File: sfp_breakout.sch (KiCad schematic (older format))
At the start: 12 parts

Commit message: Started some board layout
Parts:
- gave numbers to parts that had none: 12
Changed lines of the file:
@@
 LIBS:valves
 LIBS:visgence_parts
+LIBS:sfp_breakout-cache
 EELAYER 25 0
 EELAYER END
@@
 $EndDescr
 $Comp
-L SFP U?
+L SFP U1
 U 1 1 5A14503B
 P 2925 2550
-F 0 "U?" H 2925 3150 60  0000 C CNN
+F 0 "U1" H 2925 3150 60  0000 C CNN
 F 1 "SFP" H 2925 2000 60  0000 C CNN
 F 2 "" H 2925 2550 60  0001 C CNN
@@
 	4075 2350 4750 2350
 $Comp
-L C C?
+L C C2
 U 1 1 5A1450E2
 P 4425 2500
-F 0 "C?" H 4450 2600 50  0000 L CNN
+F 0 "C2" H 4450 2600 50  0000 L CNN
 F 1 "0.1u" H 4450 2400 50  0000 L CNN
 F 2 "" H 4463 2350 50  0001 C CNN
@@
 $EndComp
 $Comp
-L L L?
+L L L1
 U 1 1 5A14512D
 P 4900 2350
-F 0 "L?" V 4850 2350 50  0000 C CNN
+F 0 "L1" V 4850 2350 50  0000 C CNN
 F 1 "1u" V 4975 2350 50  0000 C CNN
 F 2 "" H 4900 2350 50  0001 C CNN
@@
 Connection ~ 4425 2350
 $Comp
-L C C?
+L C C1
 U 1 1 5A1451E0
 P 4275 3075
-F 0 "C?" H 4300 3175 50  0000 L CNN
+F 0 "C1" H 4300 3175 50  0000 L CNN
 F 1 "0.1u" H 4300 2975 50  0000 L CNN
 F 2 "" H 4313 2925 50  0001 C CNN
@@
 $EndComp
 $Comp
-L C C?
+L C C3
 U 1 1 5A145214
 P 4625 3075
-F 0 "C?" H 4650 3175 50  0000 L CNN
+F 0 "C3" H 4650 3175 50  0000 L CNN
 F 1 "10u" H 4650 2975 50  0000 L CNN
 F 2 "" H 4663 2925 50  0001 C CNN
@@
 Connection ~ 4275 2925
 $Comp
-L L L?
+L L L2
 U 1 1 5A14529D
 P 4900 2925
-F 0 "L?" V 4850 2925 50  0000 C CNN
+F 0 "L2" V 4850 2925 50  0000 C CNN
 F 1 "1u" V 4975 2925 50  0000 C CNN
 F 2 "" H 4900 2925 50  0001 C CNN
@@
 	5050 2350 5050 2925
 $Comp
-L C C?
+L C C4
 U 1 1 5A145370
 P 5275 3075
-F 0 "C?" H 5300 3175 50  0000 L CNN
+F 0 "C4" H 5300 3175 50  0000 L CNN
 F 1 "0.1u" H 5300 2975 50  0000 L CNN
 F 2 "" H 5313 2925 50  0001 C CNN
@@
 $EndComp
 $Comp
-L C C?
+L C C5
 U 1 1 5A1453AF
 P 5625 3075
-F 0 "C?" H 5650 3175 50  0000 L CNN
+F 0 "C5" H 5650 3175 50  0000 L CNN
 F 1 "10u" H 5650 2975 50  0000 L CNN
 F 2 "" H 5663 2925 50  0001 C CNN
@@
 Connection ~ 5275 2925
 $Comp
-L GND #PWR?
+L GND #PWR6
 U 1 1 5A14541F
 P 4275 3300
-F 0 "#PWR?" H 4275 3050 50  0001 C CNN
+F 0 "#PWR6" H 4275 3050 50  0001 C CNN
 F 1 "GND" H 4275 3150 50  0000 C CNN
 F 2 "" H 4275 3300 50  0001 C CNN
@@
 $EndComp
 $Comp
-L GND #PWR?
+L GND #PWR7
 U 1 1 5A145449
 P 4425 2700
-F 0 "#PWR?" H 4425 2450 50  0001 C CNN
+F 0 "#PWR7" H 4425 2450 50  0001 C CNN
 F 1 "GND" H 4425 2550 50  0000 C CNN
 F 2 "" H 4425 2700 50  0001 C CNN
@@
 	4425 2650 4425 2700
 $Comp
-L GND #PWR?
+L GND #PWR8
 U 1 1 5A145590
 P 4625 3300
-F 0 "#PWR?" H 4625 3050 50  0001 C CNN
+F 0 "#PWR8" H 4625 3050 50  0001 C CNN
 F 1 "GND" H 4625 3150 50  0000 C CNN
 F 2 "" H 4625 3300 50  0001 C CNN
@@
 $EndComp
 $Comp
-L GND #PWR?
+L GND #PWR9
 U 1 1 5A1455B3
 P 5275 3300
-F 0 "#PWR?" H 5275 3050 50  0001 C CNN
+F 0 "#PWR9" H 5275 3050 50  0001 C CNN
 F 1 "GND" H 5275 3150 50  0000 C CNN
 F 2 "" H 5275 3300 50  0001 C CNN
@@
 $EndComp
 $Comp
-L GND #PWR?
+L GND #PWR11
 U 1 1 5A1455D6
 P 5625 3300
-F 0 "#PWR?" H 5625 3050 50  0001 C CNN
+F 0 "#PWR11" H 5625 3050 50  0001 C CNN
 F 1 "GND" H 5625 3150 50  0000 C CNN
 F 2 "" H 5625 3300 50  0001 C CNN
@@
 	5625 3225 5625 3300
 $Comp
-L +3.3V #PWR?
+L +3.3V #PWR10
 U 1 1 5A145656
 P 5625 2675
-F 0 "#PWR?" H 5625 2525 50  0001 C CNN
+F 0 "#PWR10" H 5625 2525 50  0001 C CNN
 F 1 "+3.3V" H 5625 2815 50  0000 C CNN
 F 2 "" H 5625 2675 50  0001 C CNN
@@
 	5625 2925 5625 2675
 $Comp
-L GND #PWR?
+L GND #PWR3
 U 1 1 5A145883
 P 3700 3075
-F 0 "#PWR?" H 3700 2825 50  0001 C CNN
+F 0 "#PWR3" H 3700 2825 50  0001 C CNN
 F 1 "GND" H 3700 2925 50  0000 C CNN
 F 2 "" H 3700 3075 50  0001 C CNN
@@
 	3700 3000 3700 3075
 $Comp
-L GND #PWR?
+L GND #PWR2
 U 1 1 5A1458D2
 P 2050 3050
-F 0 "#PWR?" H 2050 2800 50  0001 C CNN
+F 0 "#PWR2" H 2050 2800 50  0001 C CNN
 F 1 "GND" H 2050 2900 50  0000 C CNN
 F 2 "" H 2050 3050 50  0001 C CNN
@@
 Connection ~ 2050 3000
 $Comp
-L GND #PWR?
+L GND #PWR1
 U 1 1 5A14597C
 P 1800 2200
-F 0 "#PWR?" H 1800 1950 50  0001 C CNN
+F 0 "#PWR1" H 1800 1950 50  0001 C CNN
 F 1 "GND" H 1800 2050 50  0000 C CNN
 F 2 "" H 1800 2200 50  0001 C CNN
@@
 	1800 2100 2175 2100
 $Comp
-L GND #PWR?
+L GND #PWR5
 U 1 1 5A1459D9
 P 4025 2150
-F 0 "#PWR?" H 4025 1900 50  0001 C CNN
+F 0 "#PWR5" H 4025 1900 50  0001 C CNN
 F 1 "GND" H 4025 2000 50  0000 C CNN
 F 2 "" H 4025 2150 50  0001 C CNN
@@
 	3675 2900 3625 2900
 $Comp
-L GND #PWR?
+L GND #PWR4
 U 1 1 5A145C02
 P 3950 3075
-F 0 "#PWR?" H 3950 2825 50  0001 C CNN
+F 0 "#PWR4" H 3950 2825 50  0001 C CNN
 F 1 "GND" H 3950 2925 50  0000 C CNN
 F 2 "" H 3950 3075 50  0001 C CNN
@@
 	3950 2700 3950 3075
 $Comp
-L Conn_Coaxial J?
+L Conn_Coaxial J1
 U 1 1 5A145ECA
 P 7650 1950
-F 0 "J?" H 7660 2070 50  0000 C CNN
+F 0 "J1" H 7660 2070 50  0000 C CNN
 F 1 "TD-" V 7765 1950 50  0000 C CNN
 F 2 "" H 7650 1950 50  0001 C CNN
@@
 $EndComp
 $Comp
-L Conn_Coaxial J?
+L Conn_Coaxial J2
 U 1 1 5A1460BD
 P 7650 2400
-F 0 "J?" H 7660 2520 50  0000 C CNN
+F 0 "J2" H 7660 2520 50  0000 C CNN
 F 1 "TD+" V 7765 2400 50  0000 C CNN
 F 2 "" H 7650 2400 50  0001 C CNN
@@
 $EndComp
 $Comp
-L Conn_Coaxial J?
+L Conn_Coaxial J3
 U 1 1 5A14613D
 P 7650 3050
-F 0 "J?" H 7660 3170 50  0000 C CNN
+F 0 "J3" H 7660 3170 50  0000 C CNN
 F 1 "RD+" V 7765 3050 50  0000 C CNN
 F 2 "" H 7650 3050 50  0001 C CNN
@@
 $EndComp
 $Comp
-L Conn_Coaxial J?
+L Conn_Coaxial J4
 U 1 1 5A1461B6
 P 7650 3525
-F 0 "J?" H 7660 3645 50  0000 C CNN
+F 0 "J4" H 7660 3645 50  0000 C CNN
 F 1 "RD-" V 7765 3525 50  0000 C CNN
 F 2 "" H 7650 3525 50  0001 C CNN
@@
 	7500 3525 7300 3525
 $Comp
-L GND #PWR?
+L GND #PWR12
 U 1 1 5A146933
 P 8025 2250
-F 0 "#PWR?" H 8025 2000 50  0001 C CNN
+F 0 "#PWR12" H 8025 2000 50  0001 C CNN
 F 1 "GND" H 8025 2100 50  0000 C CNN
 F 2 "" H 8025 2250 50  0001 C CNN
@@
 	8025 2150 8025 2250
 $Comp
-L GND #PWR?
+L GND #PWR13
 U 1 1 5A1469CA
 P 8025 2650
-F 0 "#PWR?" H 8025 2400 50  0001 C CNN
+F 0 "#PWR13" H 8025 2400 50  0001 C CNN
 F 1 "GND" H 8025 2500 50  0000 C CNN
 F 2 "" H 8025 2650 50  0001 C CNN
@@
 	8025 2600 8025 2650
 $Comp
-L GND #PWR?
+L GND #PWR14
 U 1 1 5A146A7B
 P 8025 3325
-F 0 "#PWR?" H 8025 3075 50  0001 C CNN
+F 0 "#PWR14" H 8025 3075 50  0001 C CNN
 F 1 "GND" H 8025 3175 50  0000 C CNN
 F 2 "" H 8025 3325 50  0001 C CNN
@@
 	8025 3250 8025 3325
 $Comp
-L GND #PWR?
+L GND #PWR15
 U 1 1 5A146AF2
 P 8025 3775
-F 0 "#PWR?" H 8025 3525 50  0001 C CNN
+F 0 "#PWR15" H 8025 3525 50  0001 C CNN
 F 1 "GND" H 8025 3625 50  0000 C CNN
 F 2 "" H 8025 3775 50  0001 C CNN

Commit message: Changed out SMA connector
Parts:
- C1, C2, C3, C4, C5: footprint (none) -> Capacitors_SMD:C_0603
- J1, J2, J3, J4: footprint (none) -> visgence_parts:CON-SMA-EDGE
- L1, L2: footprint (none) -> visgence_parts:SM0603_VIS
- U1: footprint (none) -> visgence_parts:UE75-A20
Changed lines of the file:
@@
 F 0 "U1" H 2925 3150 60  0000 C CNN
 F 1 "SFP" H 2925 2000 60  0000 C CNN
-F 2 "" H 2925 2550 60  0001 C CNN
+F 2 "visgence_parts:UE75-A20" H 2925 2550 60  0001 C CNN
 F 3 "" H 2925 2550 60  0001 C CNN
 	1    2925 2550
@@
 F 0 "C2" H 4450 2600 50  0000 L CNN
 F 1 "0.1u" H 4450 2400 50  0000 L CNN
-F 2 "" H 4463 2350 50  0001 C CNN
+F 2 "Capacitors_SMD:C_0603" H 4463 2350 50  0001 C CNN
 F 3 "" H 4425 2500 50  0001 C CNN
 	1    4425 2500
@@
 F 0 "L1" V 4850 2350 50  0000 C CNN
 F 1 "1u" V 4975 2350 50  0000 C CNN
-F 2 "" H 4900 2350 50  0001 C CNN
+F 2 "visgence_parts:SM0603_VIS" H 4900 2350 50  0001 C CNN
 F 3 "" H 4900 2350 50  0001 C CNN
 	1    4900 2350
@@
 F 0 "C1" H 4300 3175 50  0000 L CNN
 F 1 "0.1u" H 4300 2975 50  0000 L CNN
-F 2 "" H 4313 2925 50  0001 C CNN
+F 2 "Capacitors_SMD:C_0603" H 4313 2925 50  0001 C CNN
 F 3 "" H 4275 3075 50  0001 C CNN
 	1    4275 3075
@@
 F 0 "C3" H 4650 3175 50  0000 L CNN
 F 1 "10u" H 4650 2975 50  0000 L CNN
-F 2 "" H 4663 2925 50  0001 C CNN
+F 2 "Capacitors_SMD:C_0603" H 4663 2925 50  0001 C CNN
 F 3 "" H 4625 3075 50  0001 C CNN
 	1    4625 3075
@@
 F 0 "L2" V 4850 2925 50  0000 C CNN
 F 1 "1u" V 4975 2925 50  0000 C CNN
-F 2 "" H 4900 2925 50  0001 C CNN
+F 2 "visgence_parts:SM0603_VIS" H 4900 2925 50  0001 C CNN
 F 3 "" H 4900 2925 50  0001 C CNN
 	1    4900 2925
@@
 F 0 "C4" H 5300 3175 50  0000 L CNN
 F 1 "0.1u" H 5300 2975 50  0000 L CNN
-F 2 "" H 5313 2925 50  0001 C CNN
+F 2 "Capacitors_SMD:C_0603" H 5313 2925 50  0001 C CNN
 F 3 "" H 5275 3075 50  0001 C CNN
 	1    5275 3075
@@
 F 0 "C5" H 5650 3175 50  0000 L CNN
 F 1 "10u" H 5650 2975 50  0000 L CNN
-F 2 "" H 5663 2925 50  0001 C CNN
+F 2 "Capacitors_SMD:C_0603" H 5663 2925 50  0001 C CNN
 F 3 "" H 5625 3075 50  0001 C CNN
 	1    5625 3075
@@
 Connection ~ 5275 2925
 $Comp
-L GND #PWR6
+L GND #PWR01
 U 1 1 5A14541F
 P 4275 3300
-F 0 "#PWR6" H 4275 3050 50  0001 C CNN
+F 0 "#PWR01" H 4275 3050 50  0001 C CNN
 F 1 "GND" H 4275 3150 50  0000 C CNN
 F 2 "" H 4275 3300 50  0001 C CNN
@@
 $EndComp
 $Comp
-L GND #PWR7
+L GND #PWR02
 U 1 1 5A145449
 P 4425 2700
-F 0 "#PWR7" H 4425 2450 50  0001 C CNN
+F 0 "#PWR02" H 4425 2450 50  0001 C CNN
 F 1 "GND" H 4425 2550 50  0000 C CNN
 F 2 "" H 4425 2700 50  0001 C CNN
@@
 	4425 2650 4425 2700
 $Comp
-L GND #PWR8
+L GND #PWR03
 U 1 1 5A145590
 P 4625 3300
-F 0 "#PWR8" H 4625 3050 50  0001 C CNN
+F 0 "#PWR03" H 4625 3050 50  0001 C CNN
 F 1 "GND" H 4625 3150 50  0000 C CNN
 F 2 "" H 4625 3300 50  0001 C CNN
@@
 $EndComp
 $Comp
-L GND #PWR9
+L GND #PWR04
 U 1 1 5A1455B3
 P 5275 3300
-F 0 "#PWR9" H 5275 3050 50  0001 C CNN
+F 0 "#PWR04" H 5275 3050 50  0001 C CNN
 F 1 "GND" H 5275 3150 50  0000 C CNN
 F 2 "" H 5275 3300 50  0001 C CNN
@@
 $EndComp
 $Comp
-L GND #PWR11
+L GND #PWR05
 U 1 1 5A1455D6
 P 5625 3300
-F 0 "#PWR11" H 5625 3050 50  0001 C CNN
+F 0 "#PWR05" H 5625 3050 50  0001 C CNN
 F 1 "GND" H 5625 3150 50  0000 C CNN
 F 2 "" H 5625 3300 50  0001 C CNN
@@
 	5625 3225 5625 3300
 $Comp
-L +3.3V #PWR10
+L +3.3V #PWR06
 U 1 1 5A145656
 P 5625 2675
-F 0 "#PWR10" H 5625 2525 50  0001 C CNN
+F 0 "#PWR06" H 5625 2525 50  0001 C CNN
 F 1 "+3.3V" H 5625 2815 50  0000 C CNN
 F 2 "" H 5625 2675 50  0001 C CNN
@@
 	5625 2925 5625 2675
 $Comp
-L GND #PWR3
+L GND #PWR07
 U 1 1 5A145883
 P 3700 3075
-F 0 "#PWR3" H 3700 2825 50  0001 C CNN
+F 0 "#PWR07" H 3700 2825 50  0001 C CNN
 F 1 "GND" H 3700 2925 50  0000 C CNN
 F 2 "" H 3700 3075 50  0001 C CNN
@@
 	3700 3000 3700 3075
 $Comp
-L GND #PWR2
+L GND #PWR08
 U 1 1 5A1458D2
 P 2050 3050
-F 0 "#PWR2" H 2050 2800 50  0001 C CNN
+F 0 "#PWR08" H 2050 2800 50  0001 C CNN
 F 1 "GND" H 2050 2900 50  0000 C CNN
 F 2 "" H 2050 3050 50  0001 C CNN
@@
 Connection ~ 2050 3000
 $Comp
-L GND #PWR1
+L GND #PWR09
 U 1 1 5A14597C
 P 1800 2200
-F 0 "#PWR1" H 1800 1950 50  0001 C CNN
+F 0 "#PWR09" H 1800 1950 50  0001 C CNN
 F 1 "GND" H 1800 2050 50  0000 C CNN
 F 2 "" H 1800 2200 50  0001 C CNN
@@
 	1800 2100 2175 2100
 $Comp
-L GND #PWR5
+L GND #PWR010
 U 1 1 5A1459D9
 P 4025 2150
-F 0 "#PWR5" H 4025 1900 50  0001 C CNN
+F 0 "#PWR010" H 4025 1900 50  0001 C CNN
 F 1 "GND" H 4025 2000 50  0000 C CNN
 F 2 "" H 4025 2150 50  0001 C CNN
@@
 	3675 2900 3625 2900
 $Comp
-L GND #PWR4
+L GND #PWR011
 U 1 1 5A145C02
 P 3950 3075
-F 0 "#PWR4" H 3950 2825 50  0001 C CNN
+F 0 "#PWR011" H 3950 2825 50  0001 C CNN
 F 1 "GND" H 3950 2925 50  0000 C CNN
 F 2 "" H 3950 3075 50  0001 C CNN
@@
 F 0 "J1" H 7660 2070 50  0000 C CNN
 F 1 "TD-" V 7765 1950 50  0000 C CNN
-F 2 "" H 7650 1950 50  0001 C CNN
+F 2 "visgence_parts:CON-SMA-EDGE" H 7650 1950 50  0001 C CNN
 F 3 "" H 7650 1950 50  0001 C CNN
 	1    7650 1950
@@
 F 0 "J2" H 7660 2520 50  0000 C CNN
 F 1 "TD+" V 7765 2400 50  0000 C CNN
-F 2 "" H 7650 2400 50  0001 C CNN
+F 2 "visgence_parts:CON-SMA-EDGE" H 7650 2400 50  0001 C CNN
 F 3 "" H 7650 2400 50  0001 C CNN
 	1    7650 2400
@@
 F 0 "J3" H 7660 3170 50  0000 C CNN
 F 1 "RD+" V 7765 3050 50  0000 C CNN
-F 2 "" H 7650 3050 50  0001 C CNN
+F 2 "visgence_parts:CON-SMA-EDGE" H 7650 3050 50  0001 C CNN
 F 3 "" H 7650 3050 50  0001 C CNN
 	1    7650 3050
@@
 F 0 "J4" H 7660 3645 50  0000 C CNN
 F 1 "RD-" V 7765 3525 50  0000 C CNN
-F 2 "" H 7650 3525 50  0001 C CNN
+F 2 "visgence_parts:CON-SMA-EDGE" H 7650 3525 50  0001 C CNN
 F 3 "" H 7650 3525 50  0001 C CNN
 	1    7650 3525
@@
 	7500 3525 7300 3525
 $Comp
-L GND #PWR12
+L GND #PWR012
 U 1 1 5A146933
 P 8025 2250
-F 0 "#PWR12" H 8025 2000 50  0001 C CNN
+F 0 "#PWR012" H 8025 2000 50  0001 C CNN
 F 1 "GND" H 8025 2100 50  0000 C CNN
 F 2 "" H 8025 2250 50  0001 C CNN
@@
 	8025 2150 8025 2250
 $Comp
-L GND #PWR13
+L GND #PWR013
 U 1 1 5A1469CA
 P 8025 2650
-F 0 "#PWR13" H 8025 2400 50  0001 C CNN
+F 0 "#PWR013" H 8025 2400 50  0001 C CNN
 F 1 "GND" H 8025 2500 50  0000 C CNN
 F 2 "" H 8025 2650 50  0001 C CNN
@@
 	8025 2600 8025 2650
 $Comp
-L GND #PWR14
+L GND #PWR014
 U 1 1 5A146A7B
 P 8025 3325
-F 0 "#PWR14" H 8025 3075 50  0001 C CNN
+F 0 "#PWR014" H 8025 3075 50  0001 C CNN
 F 1 "GND" H 8025 3175 50  0000 C CNN
 F 2 "" H 8025 3325 50  0001 C CNN
@@
 	8025 3250 8025 3325
 $Comp
-L GND #PWR15
+L GND #PWR015
 U 1 1 5A146AF2
 P 8025 3775
-F 0 "#PWR15" H 8025 3525 50  0001 C CNN
+F 0 "#PWR015" H 8025 3525 50  0001 C CNN
 F 1 "GND" H 8025 3625 50  0000 C CNN
 F 2 "" H 8025 3775 50  0001 C CNN

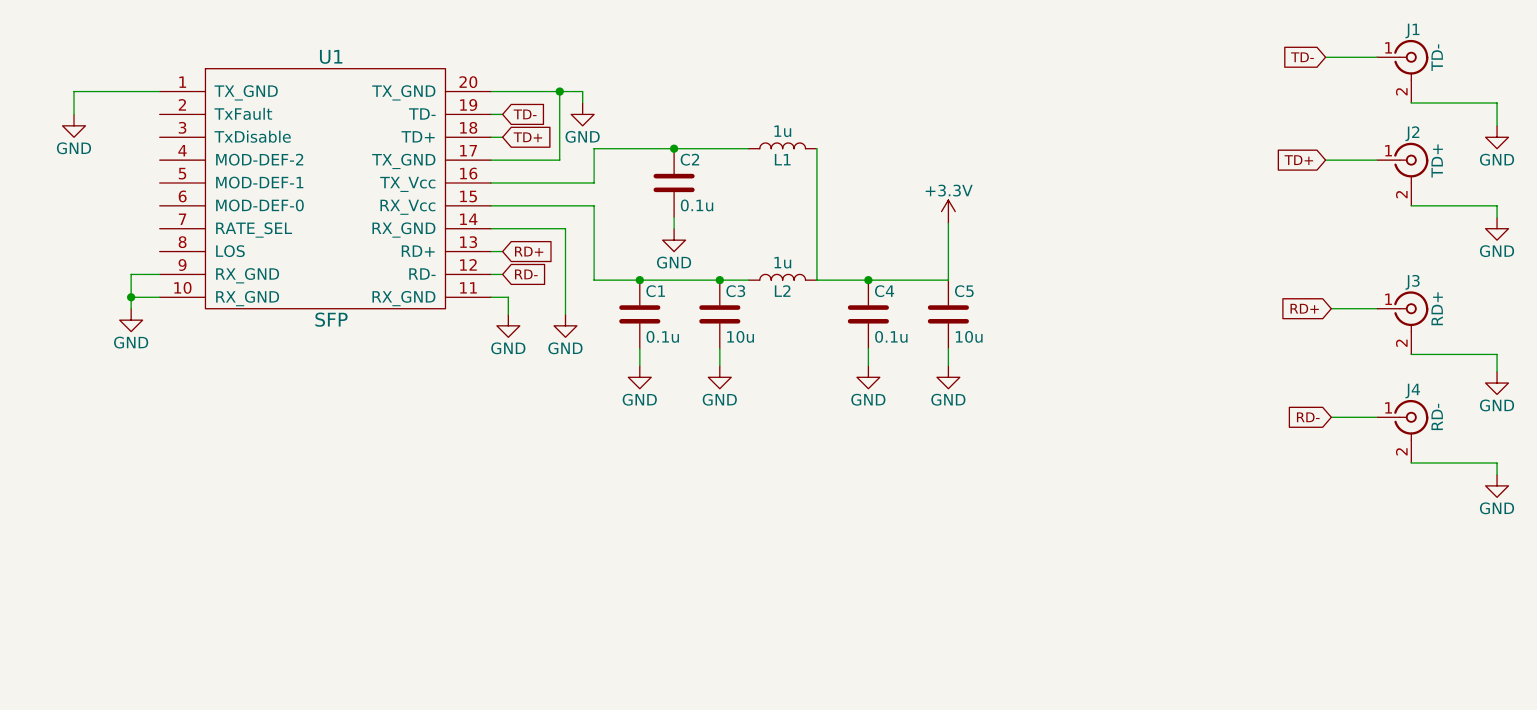
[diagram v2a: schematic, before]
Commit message: Added pin header, worked on board layout
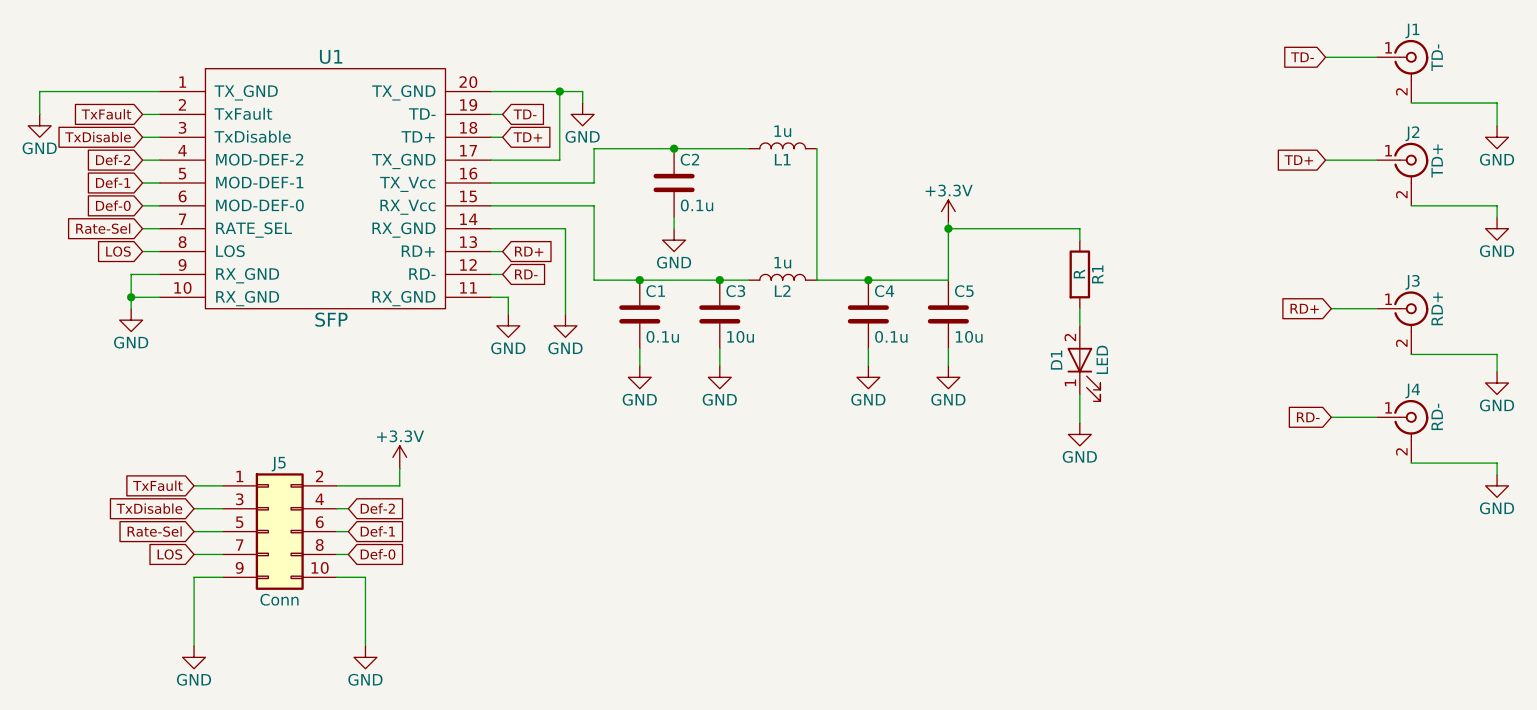
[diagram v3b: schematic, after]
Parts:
- added D1: LED, LEDs:LED_0603_HandSoldering, symbol LED
- added J5: Conn, Pin_Headers:Pin_Header_Straight_2x05_Pitch2.54mm, symbol Conn_02x05_Odd_Even
- added R1: R, visgence_parts:SM0603_VIS, symbol R
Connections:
- net +3V3: now also J5.2 (Pin_2), R1.1
- net GND: now also D1.1 (K), J5.10 (Pin_10), J5.9 (Pin_9)
- net TxFault: now reaches U1.2 (TxFault)
- net TxFault: now also J5.1 (Pin_1)
- net TxDisable: now reaches U1.3 (TxDisable)
- net TxDisable: now also J5.3 (Pin_3)
- net Def-2: now reaches U1.4 (MOD-DEF-2)
- net Def-2: now also J5.4 (Pin_4)
- net Def-1: now reaches U1.5 (MOD-DEF-1)
- net Def-1: now also J5.6 (Pin_6)
- net Def-0: now reaches U1.6 (MOD-DEF-0)
- net Def-0: now also J5.8 (Pin_8)
- net Rate-Sel: now reaches U1.7 (RATE_SEL)
- net Rate-Sel: now also J5.5 (Pin_5)
- net LOS: now reaches U1.8 (LOS)
- net LOS: now also J5.7 (Pin_7)
- new net: D1.2 (A), R1.2
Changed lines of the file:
@@
 L GND #PWR09
 U 1 1 5A14597C
-P 1800 2200
-F 0 "#PWR09" H 1800 1950 50  0001 C CNN
-F 1 "GND" H 1800 2050 50  0000 C CNN
-F 2 "" H 1800 2200 50  0001 C CNN
-F 3 "" H 1800 2200 50  0001 C CNN
-	1    1800 2200
-	1    0    0    -1
-$EndComp
-Wire Wire Line
-	1800 2200 1800 2100
-Wire Wire Line
-	1800 2100 2175 2100
+P 1650 2200
+F 0 "#PWR09" H 1650 1950 50  0001 C CNN
+F 1 "GND" H 1650 2050 50  0000 C CNN
+F 2 "" H 1650 2200 50  0001 C CNN
+F 3 "" H 1650 2200 50  0001 C CNN
+	1    1650 2200
+	1    0    0    -1
+$EndComp
+Wire Wire Line
+	1650 2200 1650 2100
+Wire Wire Line
+	1650 2100 2175 2100
 $Comp
 L GND #PWR010
@@
 Wire Wire Line
 	8025 3725 8025 3775
+$Comp
+L GND #PWR016
+U 1 1 5A347BC3
+P 2325 4525
+F 0 "#PWR016" H 2325 4275 50  0001 C CNN
+F 1 "GND" H 2325 4375 50  0000 C CNN
+F 2 "" H 2325 4525 50  0001 C CNN
+F 3 "" H 2325 4525 50  0001 C CNN
+	1    2325 4525
+	1    0    0    -1
+$EndComp
+Wire Wire Line
+	2325 4525 2325 4225
+Wire Wire Line
+	2325 4225 2450 4225
+$Comp
+L +3.3V #PWR017
+U 1 1 5A347D72
+P 3225 3750
+F 0 "#PWR017" H 3225 3600 50  0001 C CNN
+F 1 "+3.3V" H 3225 3890 50  0000 C CNN
+F 2 "" H 3225 3750 50  0001 C CNN
+F 3 "" H 3225 3750 50  0001 C CNN
+	1    3225 3750
+	1    0    0    -1
+$EndComp
+Wire Wire Line
+	2950 3825 3225 3825
+Wire Wire Line
+	3225 3825 3225 3750
+Text GLabel 2100 2200 0    43   Input ~ 0
+TxFault
+Text GLabel 2325 3825 0    43   Input ~ 0
+TxFault
+Text GLabel 2100 2300 0    43   Input ~ 0
+TxDisable
+Text GLabel 2100 2400 0    43   Input ~ 0
+Def-2
+Text GLabel 2100 2500 0    43   Input ~ 0
+Def-1
+Text GLabel 2100 2600 0    43   Input ~ 0
+Def-0
+Text GLabel 2100 2700 0    43   Input ~ 0
+Rate-Sel
+Text GLabel 2100 2800 0    43   Input ~ 0
+LOS
+Wire Wire Line
+	2100 2200 2175 2200
+Wire Wire Line
+	2175 2300 2100 2300
+Wire Wire Line
+	2175 2400 2100 2400
+Wire Wire Line
+	2175 2500 2100 2500
+Wire Wire Line
+	2175 2600 2100 2600
+Wire Wire Line
+	2175 2700 2100 2700
+Wire Wire Line
+	2175 2800 2100 2800
+Text GLabel 2325 3925 0    43   Input ~ 0
+TxDisable
+Text GLabel 3000 3925 2    43   Input ~ 0
+Def-2
+Text GLabel 3000 4025 2    43   Input ~ 0
+Def-1
+Text GLabel 3000 4125 2    43   Input ~ 0
+Def-0
+Text GLabel 2325 4025 0    43   Input ~ 0
+Rate-Sel
+Text GLabel 2325 4125 0    43   Input ~ 0
+LOS
+$Comp
+L GND #PWR018
+U 1 1 5A348BA8
+P 3075 4525
+F 0 "#PWR018" H 3075 4275 50  0001 C CNN
+F 1 "GND" H 3075 4375 50  0000 C CNN
+F 2 "" H 3075 4525 50  0001 C CNN
+F 3 "" H 3075 4525 50  0001 C CNN
+	1    3075 4525
+	1    0    0    -1
+$EndComp
+Wire Wire Line
+	2950 4225 3075 4225
+Wire Wire Line
+	3075 4225 3075 4525
+Wire Wire Line
+	2450 3825 2325 3825
+Wire Wire Line
+	2450 3925 2325 3925
+Wire Wire Line
+	2450 4025 2325 4025
+Wire Wire Line
+	2450 4125 2325 4125
+Wire Wire Line
+	2950 4125 3000 4125
+Wire Wire Line
+	2950 4025 3000 4025
+Wire Wire Line
+	2950 3925 3000 3925
+$Comp
+L LED D1
+U 1 1 5A3491BE
+P 6200 3275
+F 0 "D1" H 6200 3375 50  0000 C CNN
+F 1 "LED" H 6200 3175 50  0000 C CNN
+F 2 "LEDs:LED_0603_HandSoldering" H 6200 3275 50  0001 C CNN
+F 3 "" H 6200 3275 50  0001 C CNN
+	1    6200 3275
+	0    -1   -1   0
+$EndComp
+$Comp
+L R R1
+U 1 1 5A3492D1
+P 6200 2900
+F 0 "R1" V 6280 2900 50  0000 C CNN
+F 1 "R" V 6200 2900 50  0000 C CNN
+F 2 "visgence_parts:SM0603_VIS" V 6130 2900 50  0001 C CNN
+F 3 "" H 6200 2900 50  0001 C CNN
+	1    6200 2900
+	1    0    0    -1
+$EndComp
+Wire Wire Line
+	5625 2700 6200 2700
+Wire Wire Line
+	6200 2700 6200 2750
+Connection ~ 5625 2700
+Wire Wire Line
+	6200 3050 6200 3125
+$Comp
+L GND #PWR019
+U 1 1 5A3494E2
+P 6200 3550
+F 0 "#PWR019" H 6200 3300 50  0001 C CNN
+F 1 "GND" H 6200 3400 50  0000 C CNN
+F 2 "" H 6200 3550 50  0001 C CNN
+F 3 "" H 6200 3550 50  0001 C CNN
+	1    6200 3550
+	1    0    0    -1
+$EndComp
+Wire Wire Line
+	6200 3425 6200 3550
+$Comp
+L Conn_02x05_Odd_Even J5
+U 1 1 5A349A20
+P 2650 4025
+F 0 "J5" H 2700 4325 50  0000 C CNN
+F 1 "Conn" H 2700 3725 50  0000 C CNN
+F 2 "Pin_Headers:Pin_Header_Straight_2x05_Pitch2.54mm" H 2650 4025 50  0001 C CNN
+F 3 "" H 2650 4025 50  0001 C CNN
+	1    2650 4025
+	1    0    0    -1
+$EndComp
 $EndSCHEMATC
